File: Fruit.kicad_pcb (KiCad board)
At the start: 2 copper layers, 92 x 33.8 mm, 11 parts, among them IC1 CAM-M8C-0-10, J1 Conn_01x08_Pin, J2 Conn_01x02_Pin, J3 Conn_Coaxial, SW1 SW_SPDT, U1 MicroSD, U3 BMP180, U4 Ai-Thinker-Ra-01

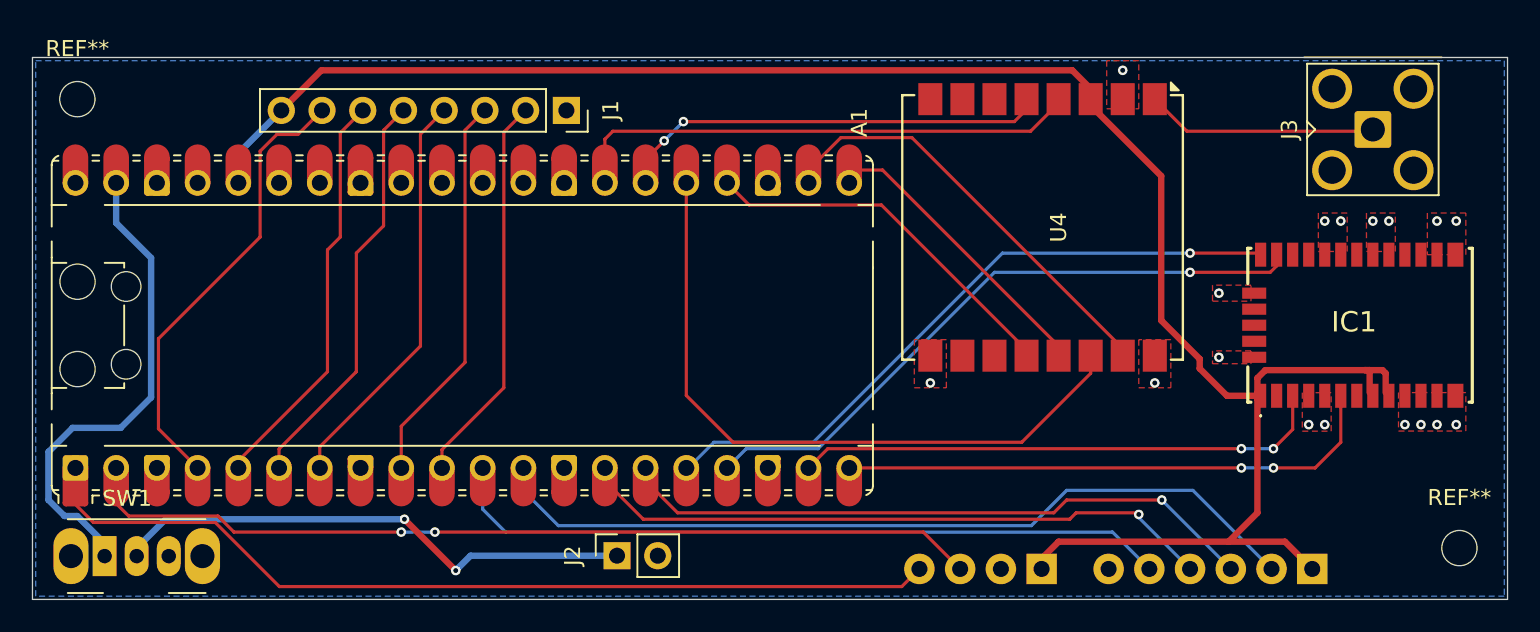
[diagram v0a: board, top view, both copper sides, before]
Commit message: feat: added silkscreen
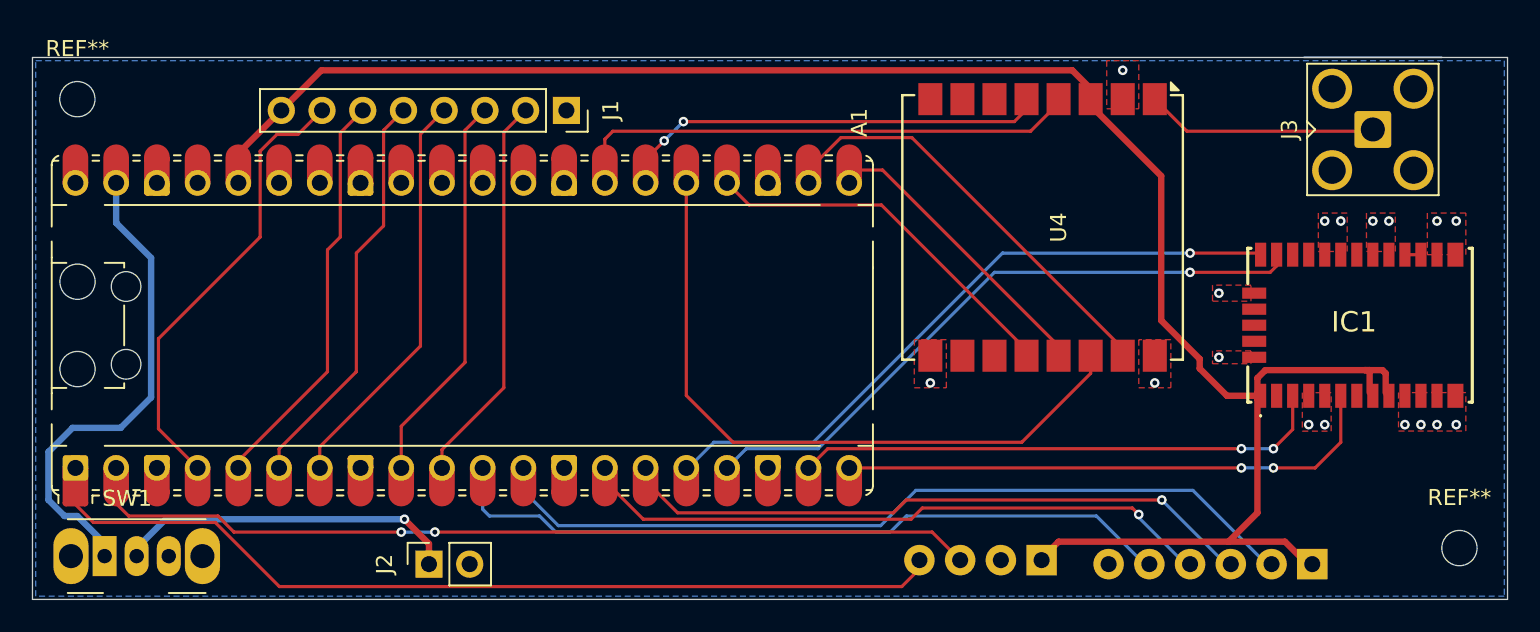
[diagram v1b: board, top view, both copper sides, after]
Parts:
- moved J2 11.7 mm to (63.7, 81.0)
- moved U3 0.55 mm to (98.1, 75.5)
- moved U1 0.30 mm to (118.8, 81.0)
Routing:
- net Net-(J2-Pin_1): track 32.9 -> 20.9 mm, vias 2 -> 1
- net /GPS_ANT: track 0.00 -> 1.00 mm
- net /SD_MISO: track 45.7 -> 46.5 mm
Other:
- board text added: "Aaron Danton (agrd2) Arin Mo (aym20)"
- board text added: "Sunrise"
